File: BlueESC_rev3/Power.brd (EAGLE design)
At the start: 24.4 x 36 mm, 47 parts, among them Q1 BC817-40W, Q2 BC817-40W, Q3 BC817-40W, Q4 SI7370, Q5 SI7370, Q6 SI7370, Q7 SI7370, Q8 SI7370, Q9 SI7370

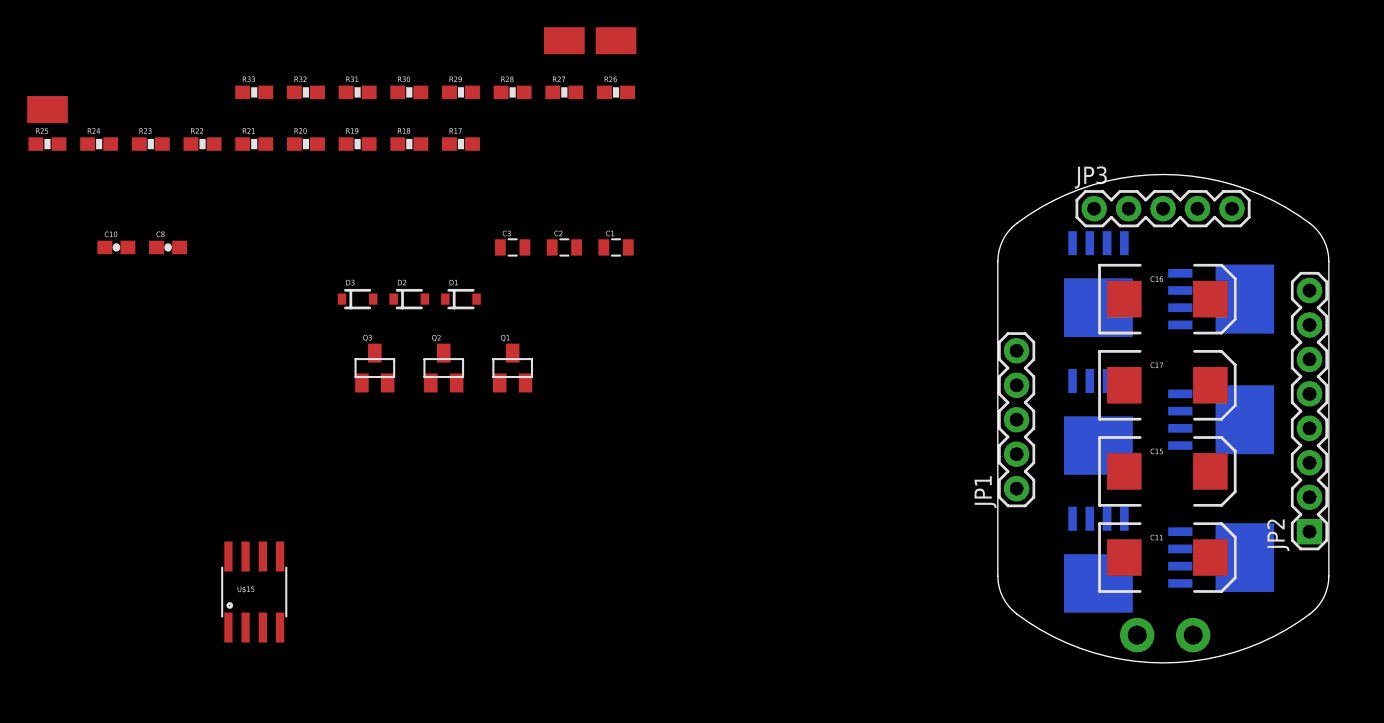
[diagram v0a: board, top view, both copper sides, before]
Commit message: Rev3 (two boards) laid out and ready to go. Final review may create a few changes.
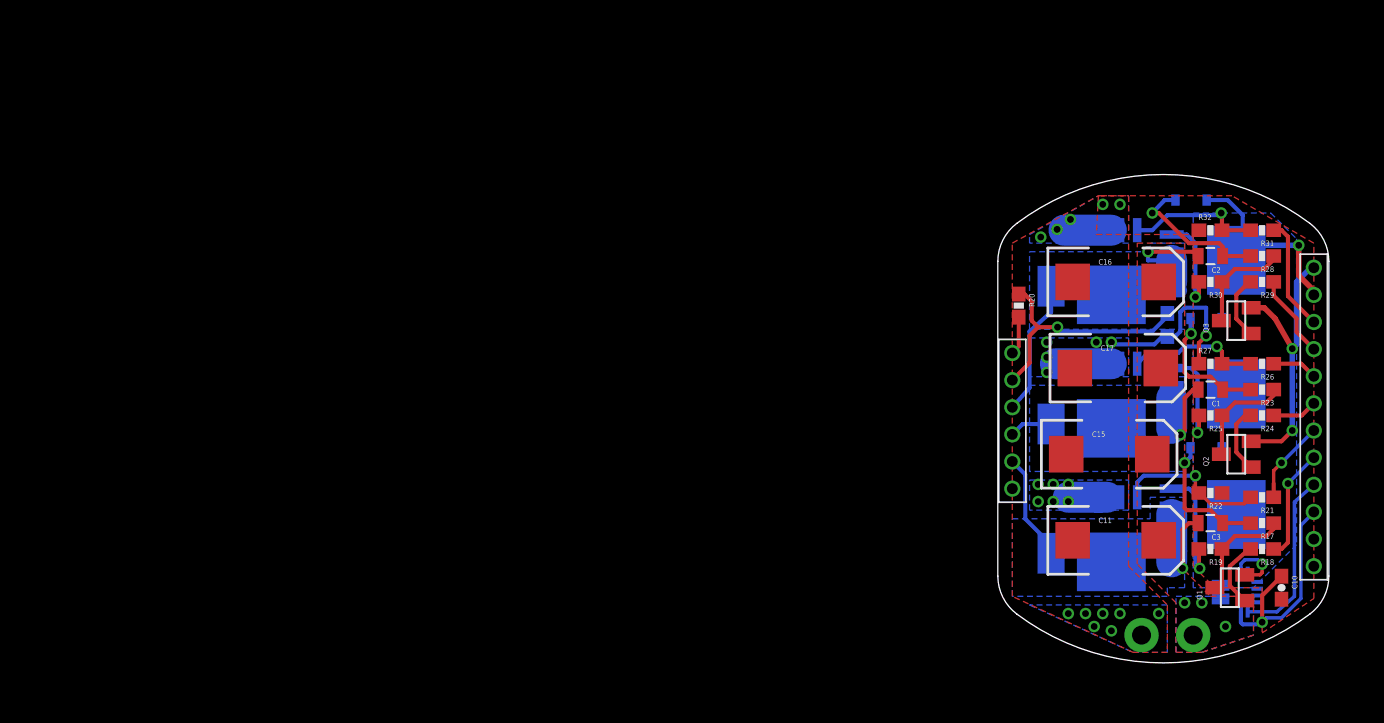
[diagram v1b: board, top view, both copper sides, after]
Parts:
- removed C8: 0.1uF, SparkFun-Capacitors:0603-CAP
- removed JP1, JP3: (no value), SparkFun-Connectors:1X05
- removed JP2: (no value), SparkFun-Connectors:1X08
- removed U$15: ACS712, SparkFun-AnalogIC:SO08
- added U$3: ACS7XX12-WFQFN, BR-Eagle-Library:12-WFQFN
- added U$4: HEADER-62MM, BR-Eagle-Library:HEADER-2MM-6POS
- added U$8: HEADER-122MM, BR-Eagle-Library:HEADER-2MM-12POS
- R33: value 10K -> 10K NTC
- moved C10 89.5 mm to (33.8, 14.3), turned to 270 degrees
- moved R24 88.0 mm to (32.4, 27.0), turned to 180 degrees
- moved R25 88.0 mm to (28.6, 27.0), turned to 180 degrees
- moved R23 83.9 mm to (32.4, 28.9), turned to 180 degrees
- moved U$5 80.9 mm to (16.8, 16.8), flipped to the bottom, turned to 270 degrees
- moved R21 78.7 mm to (32.4, 21.0), turned to 180 degrees
- moved R22 78.6 mm to (28.6, 21.3), turned to 180 degrees
- moved R18 69.6 mm to (32.4, 17.1), turned to 180 degrees
- moved R19 69.6 mm to (28.6, 17.1), turned to 180 degrees
- moved R33 69.5 mm to (25.4, 33.7), flipped to the bottom, turned to 90 degrees
- moved R31 67.4 mm to (32.4, 40.6), turned to 180 degrees
- moved R32 67.4 mm to (28.6, 40.6)
- moved R17 65.3 mm to (32.4, 19.1), turned to 180 degrees
- moved Q3 63.6 mm to (30.5, 34.0), turned to 90 degrees
- moved D3 61.9 mm to (27.1, 42.9), flipped to the bottom, turned to 180 degrees
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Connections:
- removed net N$1: C8.1, U$15.6
- removed net VCC5V: C10.1, JP3.4, R20.2, U$15.8
- new net VCC5V-1: R20.2, U$4.P$6
- new net VCC5V-2: C10.1, U$3.VCC, U$8.P$3
- net CURRENT_ADC: now also U$3.VIOUT, U$8.P$4; no longer JP3.2, U$15.7
- net GND: now also U$3.GND, U$4.P$1, U$8.P$1, U$8.P$12, U$8.P$2; no longer C8.2, JP1.1, JP1.5, JP2.1, JP2.8, JP3.5, U$15.5
- net PHASE_A: now also U$4.P$2; no longer JP1.2
- net PHASE_B: now also U$4.P$3; no longer JP1.3
- net PHASE_C: now also U$4.P$4; no longer JP1.4
- net PWM_AH: now also U$8.P$5; no longer JP2.2
- net PWM_AL: now also U$8.P$6; no longer JP2.3
- net PWM_BH: now also U$8.P$7; no longer JP2.4
- net PWM_BL: now also U$8.P$8; no longer JP2.5
- net PWM_CH: now also U$8.P$9; no longer JP2.6
- net PWM_CL: now also U$8.P$10; no longer JP2.7
- net TEMP_ADC: now also U$4.P$5; no longer JP3.1
- net VBAT: now also U$3.IP-1, U$3.IP-2, U$8.P$11; no longer C11.A, C15.A, C16.A, C17.A, JP3.3, U$15.3, U$15.4
- net VBAT+: now also C11.A, C15.A, C16.A, C17.A, U$3.IP+1, U$3.IP+2; no longer U$15.1, U$15.2
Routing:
- net GND: track 0.00 -> 50.7 mm, vias 0 -> 27
- net PHASE_C: track 0.00 -> 20.1 mm, vias 0 -> 1
- net TEMP_ADC: track 0.00 -> 18.3 mm, vias 0 -> 1
- net PHASE_A: track 0.00 -> 17.3 mm, vias 0 -> 1
- net VCC5V-2: track 0.00 -> 16.8 mm, vias 0 -> 1
- net VBAT: track 0.00 -> 14.8 mm, vias 0 -> 1
- net CURRENT_ADC: track 0.00 -> 12.7 mm
- net GATE_AL: track 0.00 -> 11.6 mm, vias 0 -> 1
- net N$19: track 0.00 -> 11.1 mm, vias 0 -> 1
- net PHASE_B: track 0.00 -> 10.3 mm, vias 0 -> 1
- net GATE_CL: track 0.00 -> 10.1 mm, vias 0 -> 1
- net N$12: track 0.00 -> 9.98 mm, vias 0 -> 1
- net GATE_BL: track 0.00 -> 9.93 mm, vias 0 -> 1
- net N$15: track 0.00 -> 9.60 mm, vias 0 -> 1
- net GATE_AH: track 0.00 -> 8.92 mm, vias 0 -> 1
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- added copper zone on layer 1, net GND
- added copper zone on layer 16, net GND
- added copper zone on layer 16, net PHASE_A
- added copper zone on layer 16, net PHASE_B
- added copper zone on layer 16, net PHASE_C
- added copper zone on layer 16, net VBAT
- added copper zone on layer 1, net VBAT+
- added copper zone on layer 16, net VBAT+
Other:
- board text added: "+"
- board text added: "-"
- board text added: "5V"
- board text added: "A"
- board text added: "AH"
- board text added: "AL"
- board text added: "B"
- board text added: "BH"
- board text added: "BL"
- board text added: "BLUESC-ELEC-POWER-XA"
- board text added: "C"
- board text added: "CH"
- board text added: "CL"
- board text added: "GND"
- board text added: "I"
- board text added: "T"
- board text added: "V+"

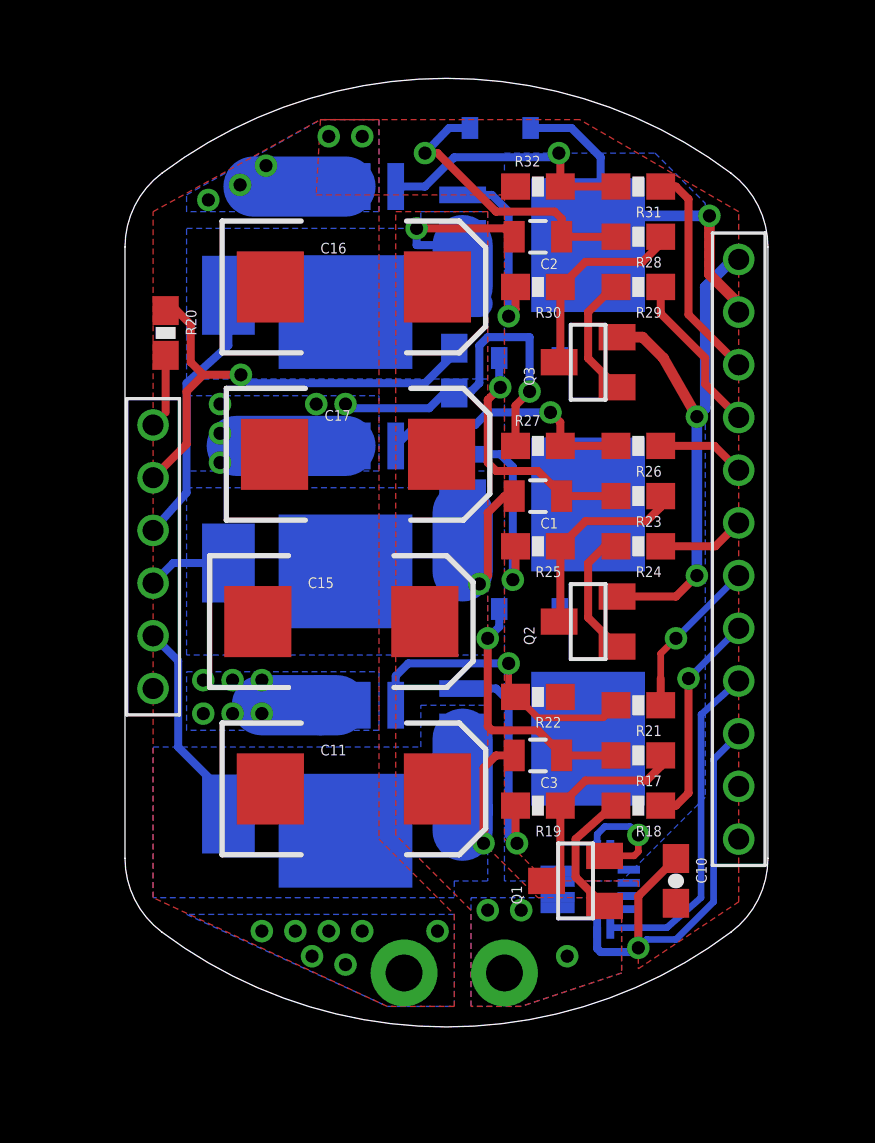
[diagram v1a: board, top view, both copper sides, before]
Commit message: Rev 3 changes. Boards have been ordered.
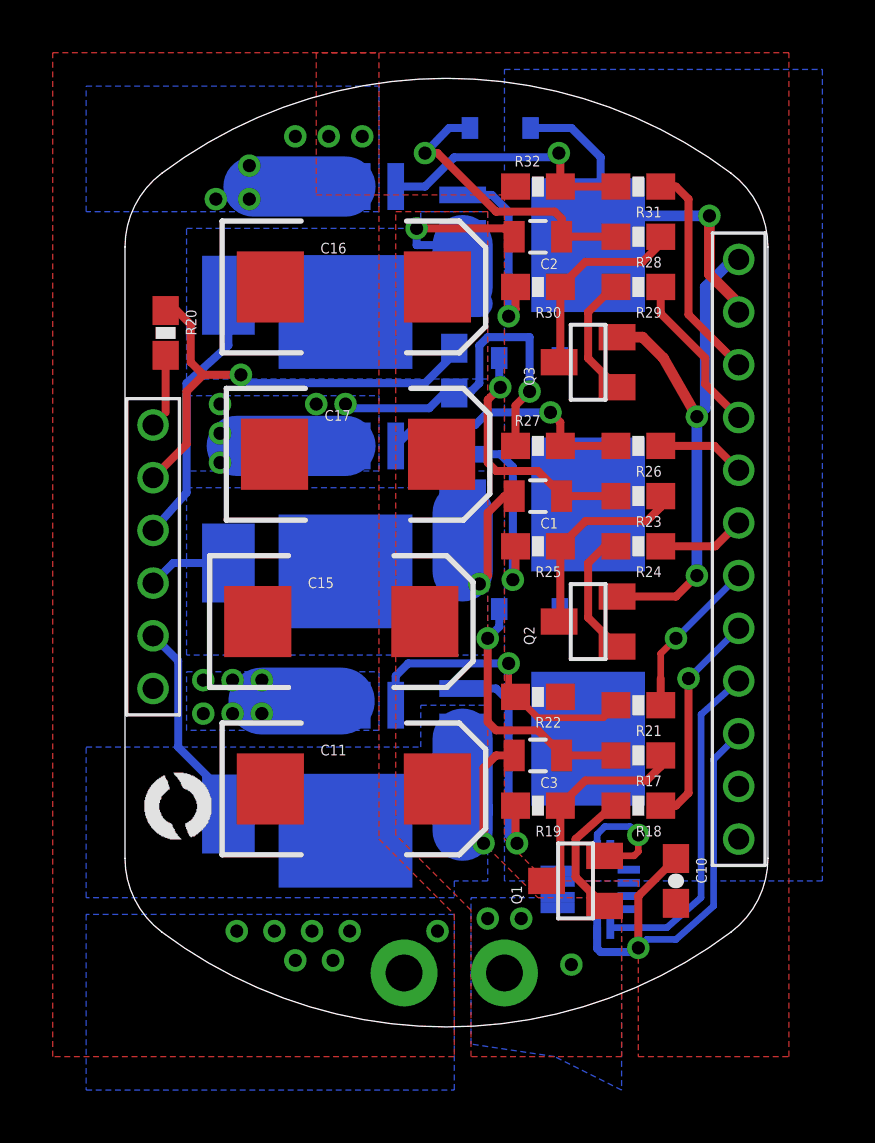
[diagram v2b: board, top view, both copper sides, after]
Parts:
- added U$9: LOGOBR-LOGO-S, BR-Eagle-Library:BR-LOGO-SMALL
- R20: value 3.3K -> 3.3K 1%
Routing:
- net GND: track 50.7 -> 50.2 mm, vias 27 -> 28
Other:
- board text added: "BLUESC-ELEC-POWER-X1A"
- board text removed: "AH"
- board text removed: "AL"
- board text removed: "BH"
- board text removed: "BL"
- board text removed: "BLUESC-ELEC-POWER-XA"
- board text removed: "CH"
- board text removed: "CL"
- board text removed: "I"
